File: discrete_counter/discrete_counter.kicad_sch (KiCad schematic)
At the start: 0 parts

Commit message: Sch: add power supply and oscillator blocks
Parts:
- added C1, C2: 10u, symbol Device:C
- added C3, C6: 0.1u, symbol Device:C
- added C4, C5: 10u, symbol Device:C_Polarized
- added D1: SS14, Diode_SMD:D_SMA, symbol Diode:SS14
- added J1: Screw_Terminal_01x02, symbol Connector:Screw_Terminal_01x02
- added Q1, Q2: 2N3904, Package_TO_SOT_THT:TO-92_Inline, symbol Transistor_BJT:2N3904
- added R1, R2: 4.7K, symbol Device:R
- added R3: 101K, symbol Device:R
- added R4: 100K, symbol Device:R
- added R5: R0, symbol Device:R
- added R6: К0, symbol Device:R
- added U1: LM7805_TO220, Package_TO_SOT_THT:TO-220-3_Vertical, symbol Regulator_Linear:LM7805_TO220
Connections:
- new net: C1.1, Q1.2 (B), R3.1
- new net: C2.1, Q1.3 (C), R2.2
- new net: C5.1, C6.1, R5.1, U1.3 (VO)
- new net: C3.1, C4.1, D1.1 (K), U1.1 (VI)
- new net: C2.2, Q2.2 (B), R4.1
- new net: C1.2, Q2.3 (C), R1.2, R6.1
- new net +12V: D1.2 (A), J1.1 (Pin_1)
- new net +5V: R1.1, R2.1, R3.2, R4.2, R5.2
- new net GND: C3.2, C4.2, C5.2, C6.2, J1.2 (Pin_2), Q1.1 (E), Q2.1 (E), U1.2 (GND)
- new net OSC_OUT: R6.2
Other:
- note added: "5V Power Supply"
- note added: "BJT Astable Multivibrator"

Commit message: m
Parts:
- added V1: 5, symbol Simulation_SPICE:VDC
- R3: value 101K -> 44k
- R4: value 100K -> 47k
- R5: value R0 -> 1R
- R6: value К0 -> 1R
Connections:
- net +5V: now also V1.1
- net GND: now also V1.2

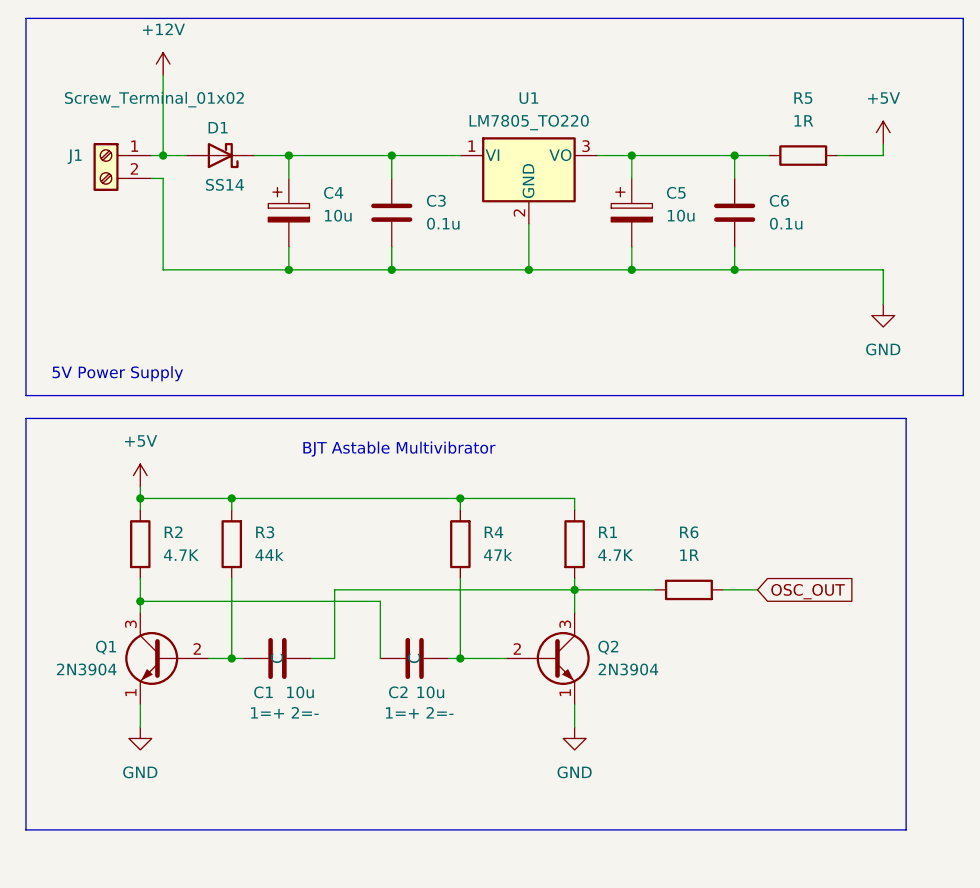
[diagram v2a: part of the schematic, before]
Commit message: Sim (oscillator) works
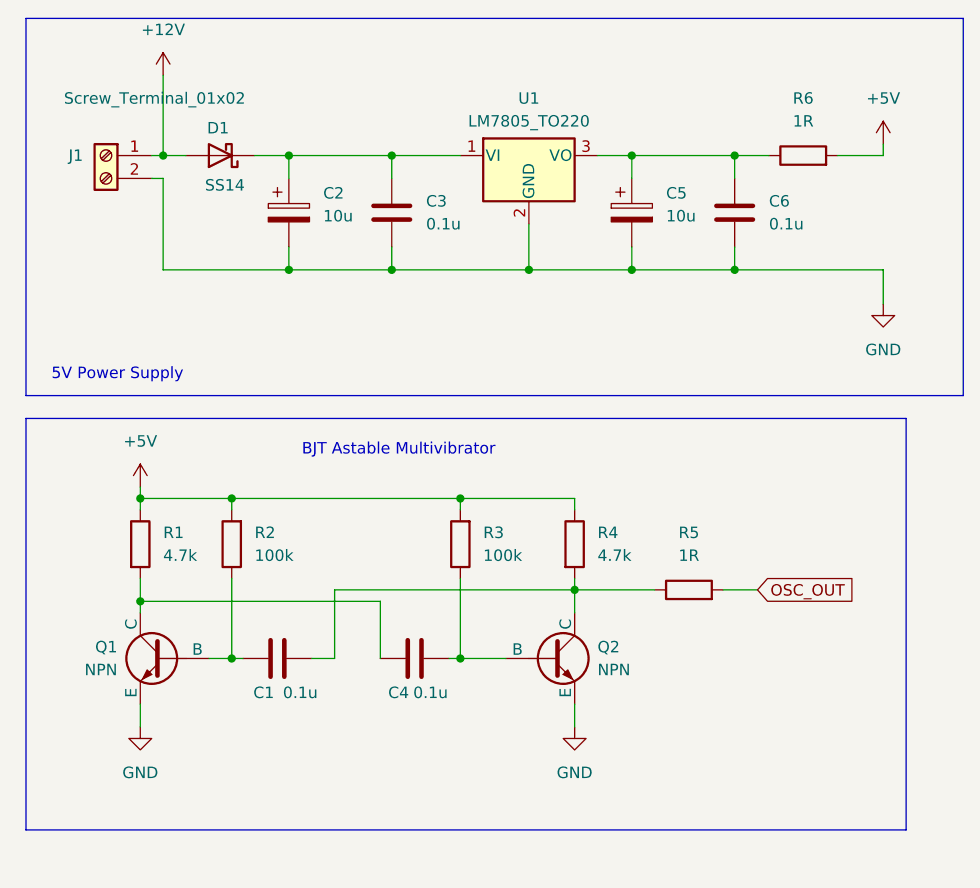
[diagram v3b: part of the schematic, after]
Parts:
- removed Q1, Q2: 2N3904, Package_TO_SOT_THT:TO-92_Inline, symbol Transistor_BJT:2N3904
- added Q1, Q2: NPN, symbol Simulation_SPICE:NPN
- C1: value 10u -> 0.1u
- C4: renamed from C2; value 10u -> 0.1u
- R1: renamed from R2; value 4.7K -> 4.7k
- R2: renamed from R3; value 44k -> 100k
- R3: renamed from R4; value 47k -> 100k
- R4: renamed from R1; value 4.7K -> 4.7k
- renumbered C4 to C2, R6 to R5, R5 to R6
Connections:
- net GND: now also Q1.3 (E), Q2.3 (E)
- net at C1.1, R2.1: now also Q1.2 (B)
- net at C4.1, R1.2: now also Q1.1 (C)
- net at C4.2, R3.1: now also Q2.2 (B)
- net at C1.2, R4.2, R5.1: now also Q2.1 (C)

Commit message: m
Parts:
- added AFF1: LTS-6980HR, Display_7Segment:7SegmentLED_LTS6760_LTS6780, symbol Display_Character:LTS-6980HR
- added C7, C8: 10p, symbol Device:C
- added Q3, Q5: PMOS, symbol Simulation_SPICE:PMOS
- added Q4, Q6: NMOS, symbol Simulation_SPICE:NMOS
- added R10, R11, R12, R20, R23, R7, R8, R9: 330R, Capacitor_SMD:C_0805_2012Metric_Pad1.18x1.45mm_HandSolder, symbol Device:R
- added R14, R15, R16, R17, R18, R19: 10k, Capacitor_SMD:C_0805_2012Metric_Pad1.18x1.45mm_HandSolder, symbol Device:R
- added R21, R22: 100k, Capacitor_SMD:C_0805_2012Metric_Pad1.18x1.45mm_HandSolder, symbol Device:R
- added U2: 4511, symbol 4xxx_IEEE:4511
- C1, C4: value 0.1u -> 10u
- J1: footprint (none) -> TerminalBlock_Phoenix:TerminalBlock_Phoenix_MKDS-1,5-2-5.08_1x02_P5.08mm_Horizontal; Digikey (none) -> https://www.digikey.com/en/products/detail/same-sky-formerl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
- R3: value 100k -> 101k
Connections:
- net +5V: now also Q3.3 (S), Q5.3 (S), R14.2, R16.2, R18.2, R20.1, U2.16 (Vdd)
- net GND: now also AFF1.3 (C.K.), AFF1.8 (C.K.), C7.2, C8.1, Q4.3 (S), Q6.3 (S), R15.1, R17.1, R19.1, R21.1, R22.1, U2.2 (DC), U2.6 (DD), U2.8 (Vss)
- net at C4.1, Q1.1 (C), R1.2: now also C8.2
- net at C1.2, Q2.1 (C), R4.2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: now also C7.1
- net OSC_OUT: no longer names the net of R5.2
- net OSC_OUT: now also Q3.2 (G), Q4.2 (G), R21.2
- new net: R7.1, U2.14 (Qg)
- new net: AFF1.10 (g), R7.2
- new net: R16.1, R17.2, U2.3 (~{LT})
- new net: R23.1, U2.13 (Qa)
- new net: AFF1.7 (a), R23.2
- new net: R14.1, R15.2, U2.4 (~{BI})
- new net: AFF1.1 (e), R9.2
- new net: AFF1.2 (d), R10.2
- new net: AFF1.4 (c), R11.2
- new net: AFF1.5 (DP), R20.2
- new net: AFF1.6 (b), R12.2
- new net: AFF1.9 (f), R8.2
- new net: R18.1, R19.2, U2.5 (~{EL})
- new net: R10.1, U2.10 (Qd)
- new net: R11.1, U2.11 (Qc)
- new net: R12.1, U2.12 (Qb)
- new net: R8.1, U2.15 (Qf)
- new net: R9.1, U2.9 (Qe)
- new net BIT0: U2.7 (DA)
- new net BIT1: U2.1 (DB)
- new net OSC_A: Q3.1 (D), Q4.1 (D), Q5.2 (G), Q6.2 (G), R22.2
- new net OSC_B: Q5.1 (D), Q6.1 (D)
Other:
- note added: "7-segment display driver"
- note added: "Power Supply"
- note removed: "5V Power Supply"
- moved on the sheet: C1, C4, Q1, Q2, R1, R2, R3, R4, R5, V1

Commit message: m
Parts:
- added Q10, Q13, Q14, Q18, Q19, Q21, Q22, Q24, Q26, Q30, Q31, Q33, Q34, Q38, Q39, Q41, Q42, Q9: NMOS, symbol Simulation_SPICE:NMOS
- added Q11, Q12, Q15, Q16, Q17, Q20, Q23, Q25, Q27, Q28, Q29, Q32, Q35, Q36, Q37, Q40, Q7, Q8: PMOS, symbol Simulation_SPICE:PMOS
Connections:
- net BIT0 is gone; now on net OSC_A: U2.7 (DA)
- net +5V: now also Q11.3 (S), Q12.3 (S), Q15.3 (S), Q16.3 (S), Q17.3 (S), Q20.3 (S), Q23.3 (S), Q25.3 (S), Q27.3 (S), Q28.3 (S), Q29.3 (S), Q32.3 (S), Q35.3 (S), Q36.3 (S), Q37.3 (S), Q40.3 (S), Q7.3 (S), Q8.3 (S)
- net GND: now also Q10.3 (S), Q14.3 (S), Q19.3 (S), Q22.3 (S), Q24.3 (S), Q26.3 (S), Q31.3 (S), Q34.3 (S), Q39.3 (S), Q42.3 (S)
- net OSC_A: now also Q28.2 (G), Q29.2 (G), Q31.2 (G), Q33.2 (G)
- net OSC_B: now also Q16.2 (G), Q17.2 (G), Q19.2 (G), Q21.2 (G)
- net BIT1 renamed Q_INV
- net Q_INV: now also Q10.2 (G), Q11.1 (D), Q12.1 (D), Q13.1 (D), Q25.2 (G), Q26.2 (G), Q27.2 (G), Q30.2 (G), Q8.2 (G)
- new net: Q18.3 (S), Q19.1 (D)
- new net: Q21.3 (S), Q22.1 (D)
- new net: Q30.3 (S), Q31.1 (D)
- new net: Q13.3 (S), Q14.1 (D)
- new net: Q20.2 (G), Q22.2 (G), Q23.1 (D), Q24.1 (D)
- new net: Q33.3 (S), Q34.1 (D)
- new net: Q36.1 (D), Q37.2 (G), Q39.2 (G), Q40.1 (D), Q41.1 (D)
- new net: Q10.1 (D), Q9.3 (S)
- new net: Q41.3 (S), Q42.1 (D)
- new net: Q25.1 (D), Q26.1 (D), Q32.2 (G), Q34.2 (G)
- new net: Q38.3 (S), Q39.1 (D)
- new net MASTER_Q: Q15.2 (G), Q18.2 (G), Q23.2 (G), Q24.2 (G), Q35.1 (D), Q36.2 (G), Q37.1 (D), Q38.1 (D), Q41.2 (G)
- new net MASTER_R_INV: Q28.1 (D), Q32.1 (D), Q33.1 (D), Q40.2 (G), Q42.2 (G)
- new net MASTER_S_INV: Q27.1 (D), Q29.1 (D), Q30.1 (D), Q35.2 (G), Q38.2 (G)
- new net Q: Q11.2 (G), Q13.2 (G), Q7.1 (D), Q8.1 (D), Q9.1 (D)
- new net SLAVE_R_INV: Q12.2 (G), Q14.2 (G), Q16.1 (D), Q20.1 (D), Q21.1 (D)
- new net SLAVE_S_INV: Q15.1 (D), Q17.1 (D), Q18.1 (D), Q7.2 (G), Q9.2 (G)
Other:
- note added: "Clocked SR latch (master)"
- note added: "Clocked SR latch (slave)"
- note added: "D-trigger"
- moved on the sheet: AFF1, R10, R11, R12, R14, R15, R16, R17, R18, R19, R20, R23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
